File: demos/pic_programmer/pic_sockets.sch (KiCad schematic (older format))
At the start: 8 parts, among them P2 SUPP28, P3 SUPP40, U1 24Cxx, U5 PIC_18_PINS, U6 PIC_8_PINS

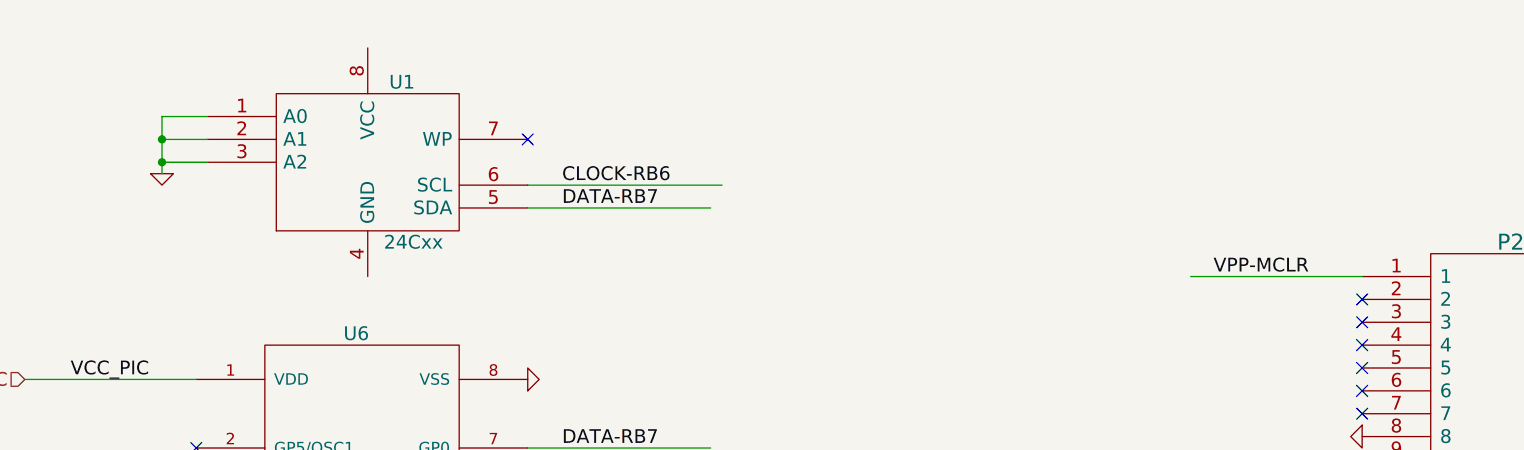
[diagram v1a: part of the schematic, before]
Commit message: Update demos. Fix  pspice netlist issues when using ( and ) in net names ( parenthesis are replaced by underscore) .
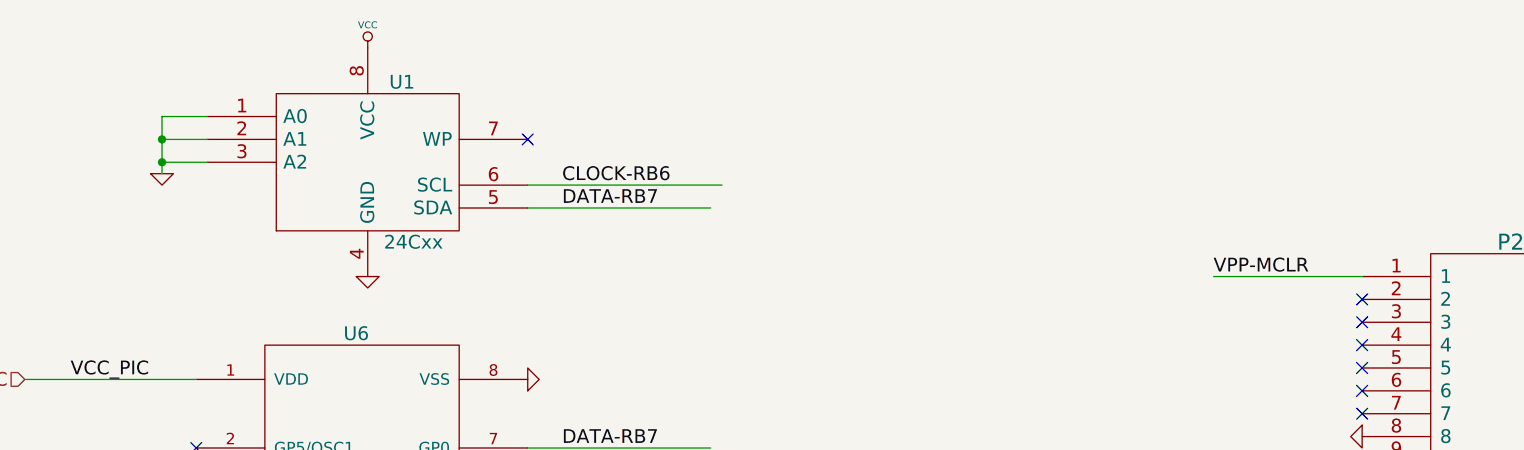
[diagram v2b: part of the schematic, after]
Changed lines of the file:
@@
 EESchema Schematic File Version 2
-LIBS:power,device,transistors,conn,linear,regul,74xx,cmos4000,adc-dac,memory,xilinx,special,microcontrollers,dsp,microchip,analog_switches,motorola,texas,intel,audio,interface,digital-audio,philips,display,cypress,siliconi,contrib,valves,.\pic_programmer.cache
-EELAYER 23  0
+LIBS:power
+LIBS:device
+LIBS:transistors
+LIBS:conn
+LIBS:linear
+LIBS:regul
+LIBS:74xx
+LIBS:cmos4000
+LIBS:adc-dac
+LIBS:memory
+LIBS:xilinx
+LIBS:special
+LIBS:microcontrollers
+LIBS:dsp
+LIBS:microchip
+LIBS:analog_switches
+LIBS:motorola
+LIBS:texas
+LIBS:intel
+LIBS:audio
+LIBS:interface
+LIBS:digital-audio
+LIBS:philips
+LIBS:display
+LIBS:cypress
+LIBS:siliconi
+LIBS:opto
+LIBS:atmel
+LIBS:pic_programmer-cache
+EELAYER 24 0
 EELAYER END
-$Descr A4 11700 8267
+$Descr A4 11693 8268
+encoding utf-8
 Sheet 2 2
 Title "JDM - COM84 PIC Programmer with 13V DC/DC converter"
@@
 Comment4 ""
 $EndDescr
-Kmarq B 3100 2150 "Warning Pin power_in non pilotée (Net 2)" F=1
 Wire Wire Line
 	3700 7000 3700 6900
@@
 	9400 1700 10200 1700
 Wire Wire Line
-	8200 1700 7450 1700
+	8200 1700 7550 1700
 Connection ~ 2950 1100
 Wire Wire Line
@@
 Connection ~ 2950 1200
 Wire Wire Line
-	2950 1250 2950 1000
+	2950 1000 2950 1250
 Wire Wire Line
 	2950 1000 3150 1000
@@
 Wire Wire Line
 	4550 6900 4550 7000
-Text Label 3950 6900 0    60   ~
+Text Label 3950 6900 0    60   ~ 0
 VCC_PIC
 $Comp
@@
 U 1 1 4639BE2E
 P 4550 7400
-F 0 "#PWR036" H 4550 7400 30  0001 C C
-F 1 "GND" H 4550 7330 30  0001 C C
+F 0 "#PWR036" H 4550 7400 30  0001 C CNN
+F 1 "GND" H 4550 7330 30  0001 C CNN
+F 2 "" H 4550 7400 60  0001 C CNN
+F 3 "" H 4550 7400 60  0001 C CNN
 	1    4550 7400
 	1    0    0    -1
@@
 U 1 1 4639BE2C
 P 4550 7200
-F 0 "C8" H 4600 7300 50  0000 L C
-F 1 "100nF" H 4600 7100 50  0000 L C
+F 0 "C8" H 4600 7300 50  0000 L CNN
+F 1 "100nF" H 4600 7100 50  0000 L CNN
+F 2 "" H 4550 7200 60  0001 C CNN
+F 3 "" H 4550 7200 60  0001 C CNN
 	1    4550 7200
 	1    0    0    -1
 $EndComp
-Text HLabel 2350 2150 0    60   Input
-VCC_PIC
-Text Label 2550 2150 0    60   ~
-VCC_PIC
-Text Label 7650 5150 0    60   ~
-VCC_PIC
-Text Label 9900 4950 0    60   ~
-VCC_PIC
-Text Label 9650 2500 0    60   ~
+Text HLabel 2350 2150 0    60   Input ~ 0
+VCC_PIC
+Text Label 2550 2150 0    60   ~ 0
+VCC_PIC
+Text Label 7650 5150 0    60   ~ 0
+VCC_PIC
+Text Label 9900 4950 0    60   ~ 0
+VCC_PIC
+Text Label 9650 2500 0    60   ~ 0
 VCC_PIC
 $Comp
@@
 U 1 1 442A8794
 P 8450 5250
-F 0 "#PWR037" H 8450 5250 30  0001 C C
-F 1 "GND" H 8450 5180 30  0001 C C
+F 0 "#PWR037" H 8450 5250 30  0001 C CNN
+F 1 "GND" H 8450 5180 30  0001 C CNN
+F 2 "" H 8450 5250 60  0001 C CNN
+F 3 "" H 8450 5250 60  0001 C CNN
 	1    8450 5250
 	0    1    1    0
 $EndComp
-Text Label 4300 4850 0    60   ~
+Text Label 4300 4850 0    60   ~ 0
 VCC_PIC
 $Comp
@@
 U 1 1 443CCA5D
 P 8450 4850
-F 0 "#PWR038" H 8450 4850 30  0001 C C
-F 1 "GND" H 8450 4780 30  0001 C C
+F 0 "#PWR038" H 8450 4850 30  0001 C CNN
+F 1 "GND" H 8450 4780 30  0001 C CNN
+F 2 "" H 8450 4850 60  0001 C CNN
+F 3 "" H 8450 4850 60  0001 C CNN
 	1    8450 4850
 	0    1    1    0
@@
 U 1 1 443697C7
 P 9400 2600
-F 0 "#PWR039" H 9400 2600 30  0001 C C
-F 1 "GND" H 9400 2530 30  0001 C C
+F 0 "#PWR039" H 9400 2600 30  0001 C CNN
+F 1 "GND" H 9400 2530 30  0001 C CNN
+F 2 "" H 9400 2600 60  0001 C CNN
+F 3 "" H 9400 2600 60  0001 C CNN
 	1    9400 2600
 	0    -1   -1   0
@@
 U 1 1 443697C3
 P 8200 2400
-F 0 "#PWR040" H 8200 2400 30  0001 C C
-F 1 "GND" H 8200 2330 30  0001 C C
+F 0 "#PWR040" H 8200 2400 30  0001 C CNN
+F 1 "GND" H 8200 2330 30  0001 C CNN
+F 2 "" H 8200 2400 60  0001 C CNN
+F 3 "" H 8200 2400 60  0001 C CNN
 	1    8200 2400
 	0    1    1    0
 $EndComp
-Text Label 9550 1800 0    60   ~
-CLOCK-RB6
-Text Label 9550 1700 0    60   ~
-DATA-RB7
-Text Label 7550 1700 0    60   ~
+Text Label 9550 1800 0    60   ~ 0
+CLOCK-RB6
+Text Label 9550 1700 0    60   ~ 0
+DATA-RB7
+Text Label 7550 1700 0    60   ~ 0
 VPP-MCLR
 $Comp
@@
 U 1 1 4436967E
 P 8800 2350
-F 0 "P2" H 8850 3150 70  0000 C C
-F 1 "SUPP28" H 8800 1550 70  0000 C C
+F 0 "P2" H 8850 3150 70  0000 C CNN
+F 1 "SUPP28" H 8800 1550 70  0000 C CNN
+F 2 "" H 8800 2350 60  0001 C CNN
+F 3 "" H 8800 2350 60  0001 C CNN
 	1    8800 2350
 	1    0    0    -1
@@
 U 1 1 442AA147
 P 3700 7400
-F 0 "#PWR041" H 3700 7400 30  0001 C C
-F 1 "GND" H 3700 7330 30  0001 C C
+F 0 "#PWR041" H 3700 7400 30  0001 C CNN
+F 1 "GND" H 3700 7330 30  0001 C CNN
+F 2 "" H 3700 7400 60  0001 C CNN
+F 3 "" H 3700 7400 60  0001 C CNN
 	1    3700 7400
 	1    0    0    -1
@@
 U 1 1 442AA145
 P 3700 7200
-F 0 "C7" H 3750 7300 50  0000 L C
-F 1 "100nF" H 3750 7100 50  0000 L C
+F 0 "C7" H 3750 7300 50  0000 L CNN
+F 1 "100nF" H 3750 7100 50  0000 L CNN
+F 2 "" H 3700 7200 60  0001 C CNN
+F 3 "" H 3700 7200 60  0001 C CNN
 	1    3700 7200
 	1    0    0    -1
@@
 U 1 1 442AA138
 P 2700 7400
-F 0 "#PWR042" H 2700 7400 30  0001 C C
-F 1 "GND" H 2700 7330 30  0001 C C
+F 0 "#PWR042" H 2700 7400 30  0001 C CNN
+F 1 "GND" H 2700 7330 30  0001 C CNN
+F 2 "" H 2700 7400 60  0001 C CNN
+F 3 "" H 2700 7400 60  0001 C CNN
 	1    2700 7400
 	1    0    0    -1
@@
 U 1 1 442AA134
 P 2700 7000
-F 0 "#PWR043" H 2700 7100 30  0001 C C
-F 1 "VCC" H 2700 7100 30  0000 C C
+F 0 "#PWR043" H 2700 7100 30  0001 C CNN
+F 1 "VCC" H 2700 7100 30  0000 C CNN
+F 2 "" H 2700 7000 60  0001 C CNN
+F 3 "" H 2700 7000 60  0001 C CNN
 	1    2700 7000
 	1    0    0    -1
@@
 U 1 1 442AA12B
 P 2700 7200
-F 0 "C6" H 2750 7300 50  0000 L C
-F 1 "100nF" H 2750 7100 50  0000 L C
+F 0 "C6" H 2750 7300 50  0000 L CNN
+F 1 "100nF" H 2750 7100 50  0000 L CNN
+F 2 "" H 2700 7200 60  0001 C CNN
+F 3 "" H 2700 7200 60  0001 C CNN
 	1    2700 7200
 	1    0    0    -1
@@
 U 1 1 442A896A
 P 9650 5050
-F 0 "#PWR044" H 9650 5050 30  0001 C C
-F 1 "GND" H 9650 4980 30  0001 C C
+F 0 "#PWR044" H 9650 5050 30  0001 C CNN
+F 1 "GND" H 9650 4980 30  0001 C CNN
+F 2 "" H 9650 5050 60  0001 C CNN
+F 3 "" H 9650 5050 60  0001 C CNN
 	1    9650 5050
 	0    -1   -1   0
@@
 U 1 1 442A88ED
 P 9050 5100
-F 0 "P3" H 9100 6200 70  0000 C C
-F 1 "SUPP40" H 8900 4000 70  0000 C C
+F 0 "P3" H 9100 6200 70  0000 C CNN
+F 1 "SUPP40" H 8900 4000 70  0000 C CNN
+F 2 "" H 9050 5100 60  0001 C CNN
+F 3 "" H 9050 5100 60  0001 C CNN
 	1    9050 5100
 	1    0    0    -1
@@
 U 1 1 442A8838
 P 2950 1250
-F 0 "#PWR045" H 2950 1250 30  0001 C C
-F 1 "GND" H 2950 1180 30  0001 C C
+F 0 "#PWR045" H 2950 1250 30  0001 C CNN
+F 1 "GND" H 2950 1180 30  0001 C CNN
+F 2 "" H 2950 1250 60  0001 C CNN
+F 3 "" H 2950 1250 60  0001 C CNN
 	1    2950 1250
 	1    0    0    -1
 $EndComp
-Text Label 4700 1400 0    60   ~
-DATA-RB7
-Text Label 4700 1300 0    60   ~
+Text Label 4700 1400 0    60   ~ 0
+DATA-RB7
+Text Label 4700 1300 0    60   ~ 0
 CLOCK-RB6
 $Comp
@@
 U 1 1 442A87F7
 P 3850 1200
-F 0 "U1" H 4000 1550 60  0000 C C
-F 1 "24Cxx" H 4050 850 60  0000 C C
+F 0 "U1" H 4000 1550 60  0000 C CNN
+F 1 "24Cxx" H 4050 850 60  0000 C CNN
+F 2 "" H 3850 1200 60  0001 C CNN
+F 3 "" H 3850 1200 60  0001 C CNN
 	1    3850 1200
 	1    0    0    -1
 $EndComp
-Text Label 9800 4250 0    60   ~
-CLOCK-RB6
-Text Label 9800 4150 0    60   ~
-DATA-RB7
-Text Label 7800 4150 0    60   ~
+Text Label 9800 4250 0    60   ~ 0
+CLOCK-RB6
+Text Label 9800 4150 0    60   ~ 0
+DATA-RB7
+Text Label 7800 4150 0    60   ~ 0
 VPP-MCLR
 NoConn ~ 2500 4400
@@
 U 1 1 442A81A7
 P 3300 4850
-F 0 "U5" H 3600 5650 60  0000 C C
-F 1 "PIC_18_PINS" H 3750 4050 60  0000 C C
+F 0 "U5" H 3600 5650 60  0000 C CNN
+F 1 "PIC_18_PINS" H 3750 4050 60  0000 C CNN
+F 2 "" H 3300 4850 60  0001 C CNN
+F 3 "" H 3300 4850 60  0001 C CNN
 	1    3300 4850
 	1    0    0    -1
@@
 NoConn ~ 3100 2850
 NoConn ~ 3100 2450
-Text Label 4200 5150 0    60   ~
-CLOCK-RB6
-Text Label 4200 5000 0    60   ~
-DATA-RB7
-Text Label 1850 4700 0    60   ~
+Text Label 4200 5150 0    60   ~ 0
+CLOCK-RB6
+Text Label 4200 5000 0    60   ~ 0
+DATA-RB7
+Text Label 1850 4700 0    60   ~ 0
 VPP-MCLR
-Text Label 2450 3150 0    60   ~
+Text Label 2450 3150 0    60   ~ 0
 VPP-MCLR
-Text Label 4700 2850 0    60   ~
-CLOCK-RB6
-Text Label 4700 2450 0    60   ~
-DATA-RB7
-Text HLabel 1350 4450 0    60   Input
+Text Label 4700 2850 0    60   ~ 0
+CLOCK-RB6
+Text Label 4700 2450 0    60   ~ 0
+DATA-RB7
+Text HLabel 1350 4450 0    60   Input ~ 0
 VPP-MCLR
-Text HLabel 1350 4250 0    60   Input
-CLOCK-RB6
-Text HLabel 1350 4050 0    60   Input
+Text HLabel 1350 4250 0    60   Input ~ 0
+CLOCK-RB6
+Text HLabel 1350 4050 0    60   Input ~ 0
 DATA-RB7
 $Comp
@@
 U 1 1 442A820F
 P 2300 4900
-F 0 "#PWR046" H 2300 4900 30  0001 C C
-F 1 "GND" H 2300 4830 30  0001 C C
+F 0 "#PWR046" H 2300 4900 30  0001 C CNN
+F 1 "GND" H 2300 4830 30  0001 C CNN
+F 2 "" H 2300 4900 60  0001 C CNN
+F 3 "" H 2300 4900 60  0001 C CNN
 	1    2300 4900
 	1    0    0    -1
@@
 U 1 1 442A8205
 P 4550 2150
-F 0 "#PWR047" H 4550 2150 30  0001 C C
-F 1 "GND" H 4550 2080 30  0001 C C
+F 0 "#PWR047" H 4550 2150 30  0001 C CNN
+F 1 "GND" H 4550 2080 30  0001 C CNN
+F 2 "" H 4550 2150 60  0001 C CNN
+F 3 "" H 4550 2150 60  0001 C CNN
 	1    4550 2150
 	0    -1   -1   0
@@
 U 1 1 442A81A5
 P 3850 2650
-F 0 "U6" H 3800 3350 60  0000 C C
-F 1 "PIC_8_PINS" H 3850 1950 60  0000 C C
+F 0 "U6" H 3800 3350 60  0000 C CNN
+F 1 "PIC_8_PINS" H 3850 1950 60  0000 C CNN
+F 2 "" H 3850 2650 60  0001 C CNN
+F 3 "" H 3850 2650 60  0001 C CNN
 	1    3850 2650
 	1    0    0    -1
 $EndComp
+$Comp
+L GND #PWR048
+U 1 1 52C92629
+P 3850 1700
+F 0 "#PWR048" H 3850 1700 30  0001 C CNN
+F 1 "GND" H 3850 1630 30  0001 C CNN
+F 2 "" H 3850 1700 60  0001 C CNN
+F 3 "" H 3850 1700 60  0001 C CNN
+	1    3850 1700
+	1    0    0    -1
+$EndComp
+$Comp
+L VCC #PWR049
+U 1 1 52C92634
+P 3850 700
+F 0 "#PWR049" H 3850 800 30  0001 C CNN
+F 1 "VCC" H 3850 800 30  0000 C CNN
+F 2 "" H 3850 700 60  0001 C CNN
+F 3 "" H 3850 700 60  0001 C CNN
+	1    3850 700
+	1    0    0    -1
+$EndComp
